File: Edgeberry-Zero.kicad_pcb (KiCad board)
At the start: 2 copper layers, 92.5 x 90 mm, 52 parts, among them J1 Molex_KK_1x02_P2.54mm, J2 Raspberry_Pi_2_3, J3 Edgeberry Cartridge Connector, P1 12Vin, Q1 BC547, Q2 BC547, Q3 BC547, SW1 SW_PUSH, U1 24LC256, U2 LM2596S-5.0

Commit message: Finished design
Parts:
- removed the REF** at (83.7, 38.3)
- added J4: Conn_01x04_Pin, Connector_PinHeader_2.54mm:PinHeader_1x04_P2.54mm_Horizontal, B.Cu at (132.8, 122.9)
- G*** (x3): moved to F.Cu
- R7, R8: value 270R -> 22R
- moved G*** 146.1 mm to (154.6, 81.0)
- moved G*** 75.2 mm to (159.5, 137.2), turned to 180 degrees
- moved G*** 45.4 mm to (164.6, 84.3)
- moved R6 34.1 mm to (149.7, 127.3), turned to 180 degrees
- moved R8 34.1 mm to (149.7, 118.3), turned to 0 degrees
- moved Q2 34.0 mm to (149.6, 122.8), turned to 0 degrees
- moved R4 23.1 mm to (149.6, 99.3), turned to 180 degrees
- moved R9 21.6 mm to (149.6, 89.3)
- moved R5 19.8 mm to (149.6, 113.3), turned to 180 degrees
- moved R7 19.8 mm to (149.6, 104.3), turned to 0 degrees
- moved Q3 19.8 mm to (149.6, 108.8), turned to 0 degrees
- moved G*** 19.3 mm to (132.1, 93.7), turned to -90 degrees
- moved Q1 16.8 mm to (149.6, 94.3)
- moved R10 13.4 mm to (135.7, 114.9), turned to 180 degrees
- moved JP1 11.0 mm to (136.5, 120.9)
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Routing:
- net +3V3: track 16.4 -> 112.3 mm, vias 0 -> 2
- net +5V: track 0.00 -> 88.4 mm
- net btn_1: track 0.00 -> 77.4 mm, vias 0 -> 1
- net Net-(D1-A2): track 0.00 -> 59.9 mm, vias 0 -> 1
- net Net-(D1-A1): track 0.00 -> 46.2 mm, vias 0 -> 1
- net Net-(Q1-C): track 0.00 -> 33.9 mm, vias 0 -> 1
- net buzzer: track 0.00 -> 30.6 mm
- net ID_SDA: track 12.0 -> 33.2 mm, vias 0 -> 1
- net ID_SCL: track 9.01 -> 28.2 mm, vias 0 -> 1
- net LED_red: track 0.00 -> 16.0 mm
- net WP: track 0.00 -> 10.2 mm
- net Net-(Q3-E): track 0.00 -> 6.61 mm
- net Net-(Q2-E): track 0.00 -> 6.23 mm
- net LED_green: track 0.00 -> 5.77 mm
- net Net-(Q1-B): track 0.00 -> 4.77 mm
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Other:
- outline, holes or cut-outs redrawn
- board text added: "BTN"
- board text added: "EXP"
- board text added: "HARDWARE CARTRIDGE SLOT"
- board text added: "OPEN SOURCE HARDWARE"
- board text added: "PWR IN"
- board text added: "STATUS"
- board text removed: "Button"
- board text removed: "HARDWARE CARTRIDGE"
- board text removed: "Status LED"

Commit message: uniformity
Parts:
- removed the G*** at (132.1, 93.7)
- removed the G*** at (132.3, 83.1)
- removed the G*** at (131.8, 88.3)
- added G***: LOGO, LOGO, F.Cu at (131.7, 87.3)
- added G***: LOGO, LOGO, F.Cu at (131.4, 82.6)
- added G***: LOGO, LOGO, F.Cu at (131.4, 93.5)
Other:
- board text added: "2025"
- board text added: "RoHS"

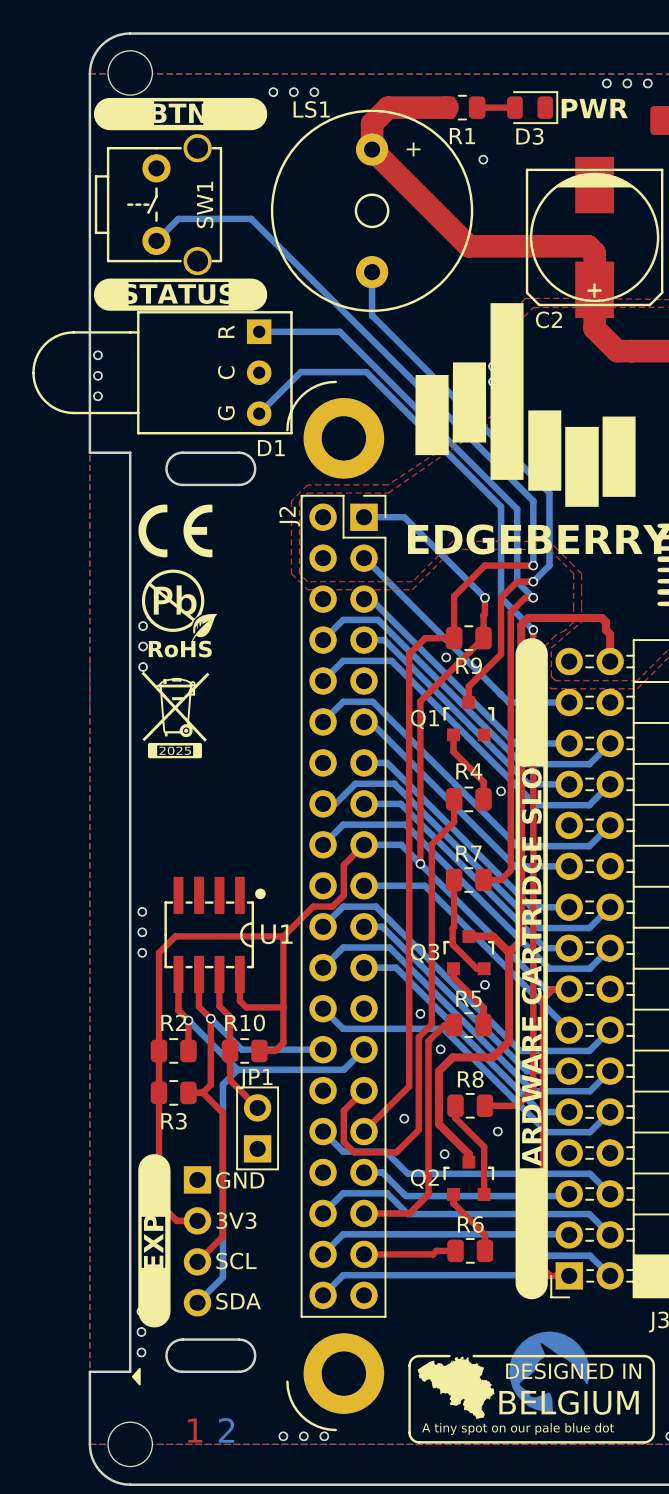
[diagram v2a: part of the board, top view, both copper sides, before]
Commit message: Improvements: C2, J4 (ext)
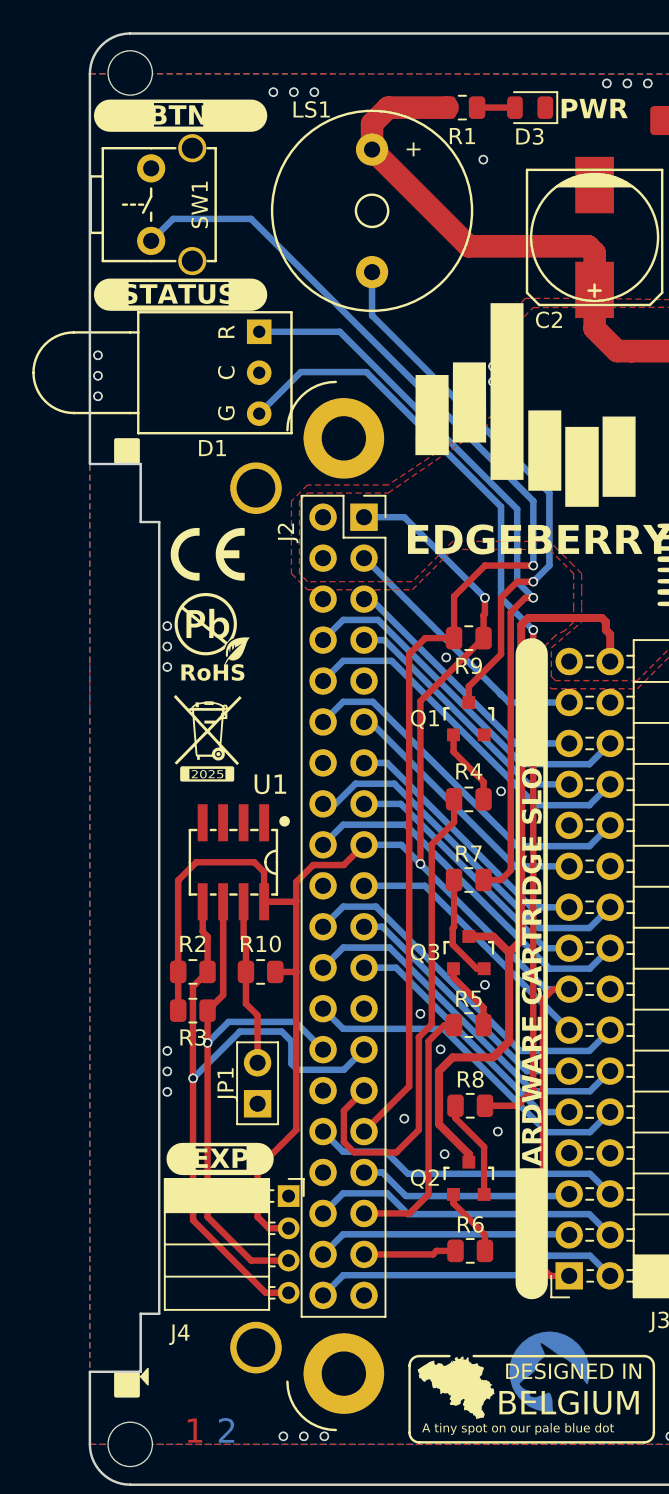
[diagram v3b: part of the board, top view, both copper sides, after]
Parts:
- added REF**: TestPoint_THTPad_2.5x2.5mm_Drill1.2mm, TestPoint:TestPoint_THTPad_2.5x2.5mm_Drill1.2mm, F.Cu at (136.4, 80.0)
- added REF**: TestPoint_THTPad_2.5x2.5mm_Drill1.2mm, TestPoint:TestPoint_THTPad_2.5x2.5mm_Drill1.2mm, F.Cu at (136.4, 133.3)
- C2: value 330uF -> 220uF
- J4: value Conn_01x04_Pin -> Conn_01x04_Socket; footprint Connector_PinHeader_2.54mm:PinHeader_1x04_P2.54mm_Horizontal -> Connector_PinSocket_2.00mm:PinSocket_1x04_P2.00mm_Horizontal; moved to F.Cu
- R1: value 270R -> 470R
- moved J4 5.74 mm to (138.5, 123.9), turned to 0 degrees
- moved R3 5.24 mm to (132.5, 112.4)
- moved R2 5.04 mm to (132.5, 110.0)
- moved R10 5.00 mm to (136.7, 110.0)
- moved U1 4.74 mm to (135.0, 103.2)
- moved G*** 2.80 mm to (136.6, 99.4)
- moved JP1 2.80 mm to (136.5, 118.1)
- moved G*** 2.49 mm to (133.7, 88.8)
- moved G*** 2.47 mm to (133.4, 84.1)
- moved G*** 2.47 mm to (133.4, 95.0)
- moved SW1 0.33 mm to (129.9, 62.4)
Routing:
- net ID_SDA: track 33.2 -> 42.2 mm
- net ID_SCL: track 28.2 -> 34.5 mm
- net GPIO_23: track 22.6 -> 21.8 mm
- net +3V3: track 112.3 -> 112.9 mm
- net GPIO_27: track 16.4 -> 15.9 mm
- net GND: vias 69 -> 66
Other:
- outline, holes or cut-outs redrawn
- board text added: "EDGEBERRY™ ZERO BOARD REVISION 1.8 BY SANNE 'SPUQ' SANTENS, EARLY 2025"
- board text added: "Rev. 1.8, early 2025"
- board text removed: "Rev. 1.7, early 2025"

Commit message: Rev 1.8
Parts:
- J4: moved to B.Cu
- moved J4 6.00 mm to (138.5, 129.9)
- moved G*** 0.70 mm to (159.5, 136.5)
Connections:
- net +12V renamed +Vin
- J4 pad 1: GND -> ID_SDA
- J4 pad 2: +3V3 -> ID_SCL
- J4 pad 3: ID_SCL -> +3V3
- J4 pad 4: ID_SDA -> GND
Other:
- board text added: "BASE BOARD Rev. 1.8, early 2025"
- board text added: "EDGEBERRY™ ZERO BASE BOARD REVISION 1.8 BY SANNE 'SPUQ' SANTENS, EARLY 2025"
- board text removed: "EDGEBERRY™ ZERO BOARD REVISION 1.8 BY SANNE 'SPUQ' SANTENS, EARLY 2025"
- board text removed: "Rev. 1.8, early 2025"
